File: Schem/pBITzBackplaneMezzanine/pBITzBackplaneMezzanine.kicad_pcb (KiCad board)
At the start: 4 copper layers, 139 x 130 mm, 52 parts, among them J1 USB3_A_Stacked, J2 Conn_01x04, J3 Conn_01x04, J4 10067847-001RLF, J5 FH69-60S-0.5SH, J6 pBITzBus, J7 FH69-60S-0.5SH, SW1 SW_Coded_SH-7030, SW2 SW_Coded_SH-7030, U1 FE1.1S-BSOP28BCN, U2 MAX3421EETJ_T, U3 CD74HC4050M96, U4 CD74HC4050M96, U5 74HC688, U6 74HC688, Y1 ABL-12.000MHZ-B2, Y2 ABL-12.000MHZ-B2

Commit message: synching
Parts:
- J2, J3: footprint Connector_PinSocket_2.54mm:PinSocket_1x04_P2.54mm_Vertical -> Connector_PinHeader_2.54mm:PinHeader_1x04_P2.54mm_Vertical

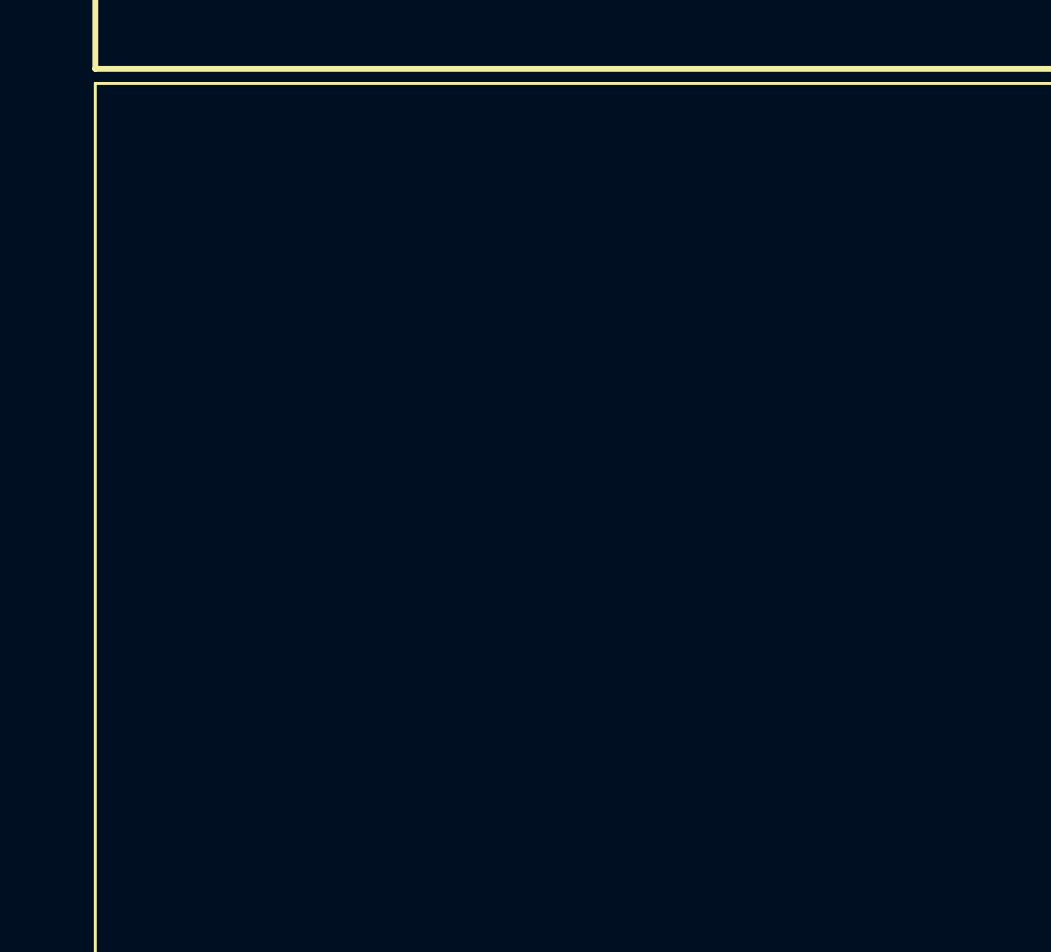
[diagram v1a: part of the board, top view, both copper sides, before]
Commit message: Added all the manufacturer part numbers to the KiCad schematics and PCB files. This will make it easier to order the parts for the project and ensure that the correct components are used. I also removed some of the old schematics that were no longer needed, such as the BaudClock, ConsolePort, DeviceSelectDecode, GPIOUserSerial, IO Controller, UserPorts, Video, and Z80HomeBrew schematics. These changes will help to streamline the design and make it easier to understand.
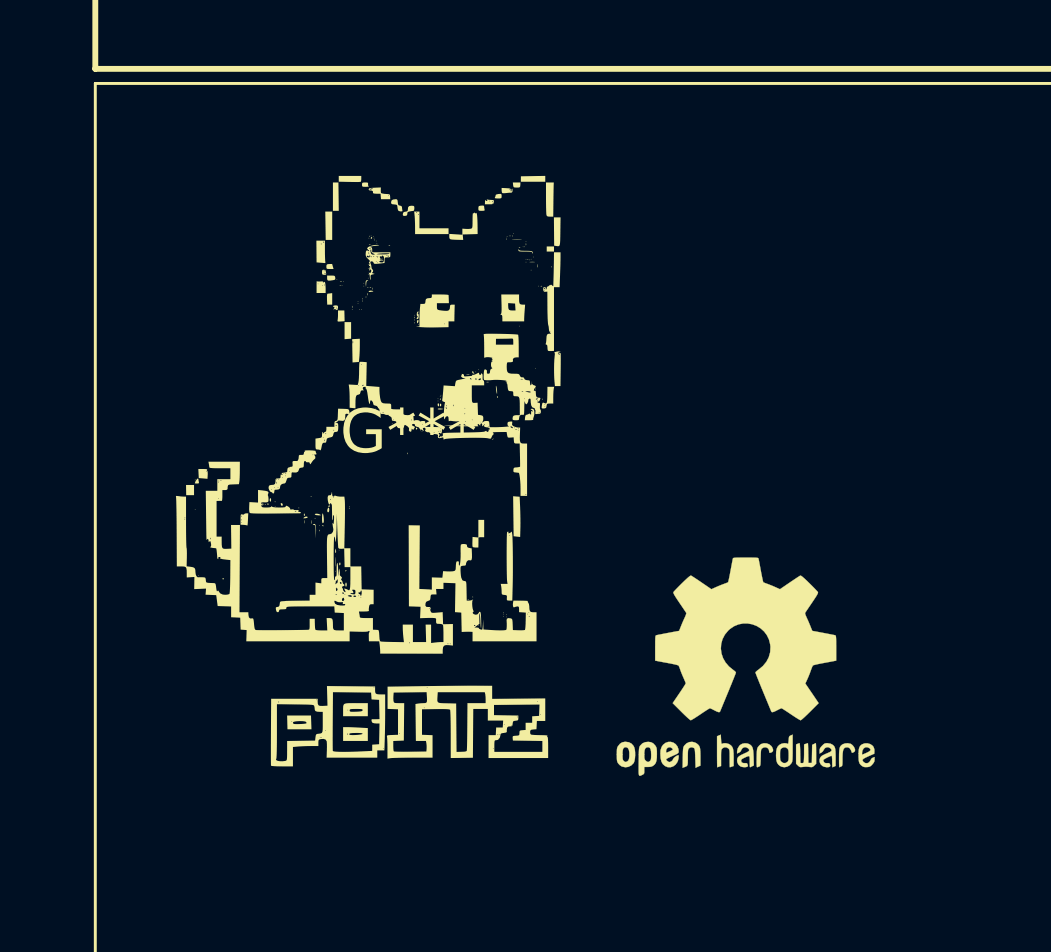
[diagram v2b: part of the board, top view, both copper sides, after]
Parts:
- added G***: LOGO, Footprints:pBITzlogo-Silk, F.Cu at (329.5, 232.5)
- added REF**: OSHW-Logo2_9.8x8mm_SilkScreen, Symbol:OSHW-Logo2_9.8x8mm_SilkScreen, F.Cu at (341.0, 240.5)

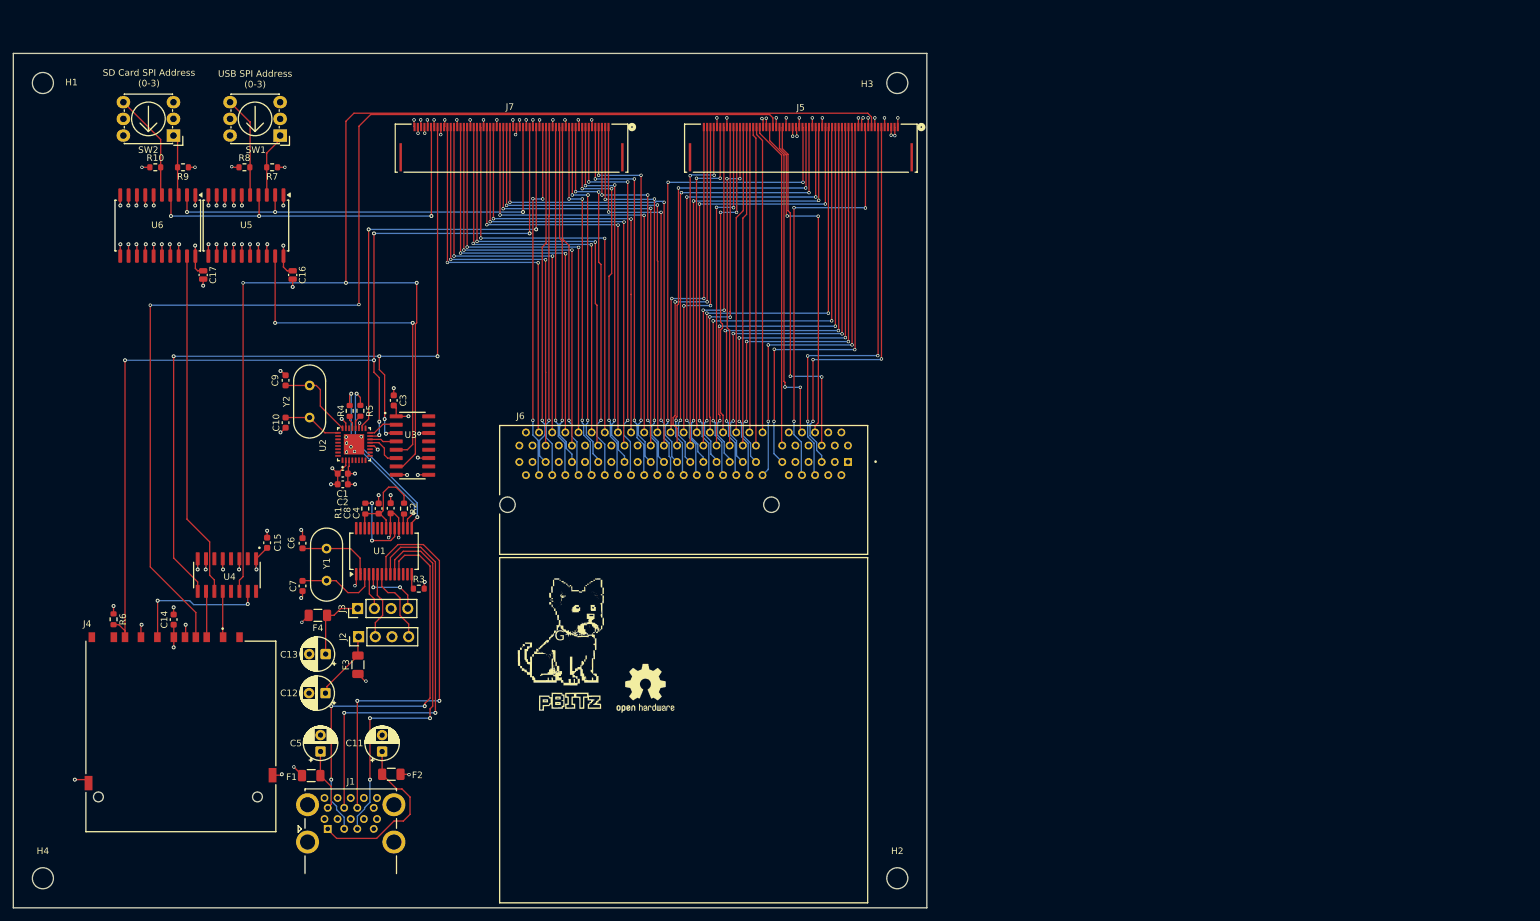
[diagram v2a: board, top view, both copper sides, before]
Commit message: * Corrected the reversal of the flat connector cable  * Added copper pours
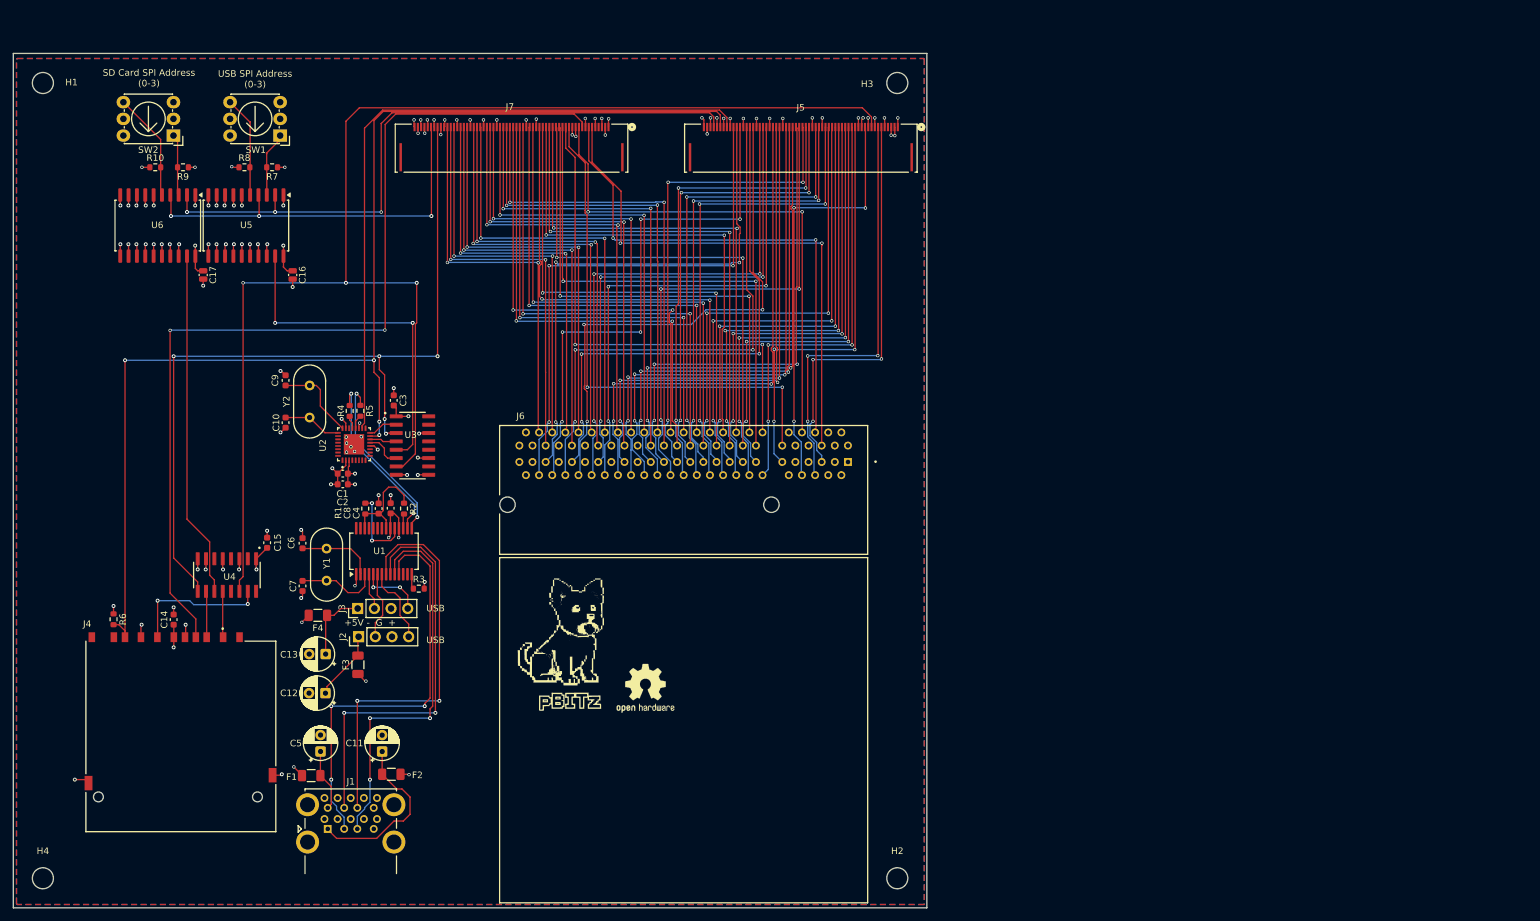
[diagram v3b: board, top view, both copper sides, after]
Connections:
- J5 pad 31: GND -> /MezzanineConnector/D11
- J5 pad 32: +5V -> /MezzanineConnector/D12
- J5 pad 33: +5V -> /MezzanineConnector/D13
- J5 pad 34: unconnected-(J5-Pad34) -> /MezzanineConnector/D14
- J5 pad 35: GND -> /MezzanineConnector/D15
- J5 pad 36: /MezzanineConnector/CLK0 -> GND
- J5 pad 37: /MezzanineConnector/CLK1 -> /MezzanineConnector/A12
- J5 pad 38: GND -> /MezzanineConnector/A13
- J5 pad 39: /MezzanineConnector/SPI_CD -> /MezzanineConnector/A14
- J5 pad 40: /MezzanineConnector/CART -> GND
- J5 pad 41: +3V3 -> /MezzanineConnector/A15
- J5 pad 42: +3V3 -> /MezzanineConnector/A16
- J5 pad 43: /MezzanineConnector/~{RESET} -> /MezzanineConnector/A17
- J5 pad 44: /MezzanineConnector/CTRL_1 -> GND
- J5 pad 45: /MezzanineConnector/CTRL_2 -> /MezzanineConnector/A18
- J5 pad 46: /MezzanineConnector/CTRL_3 -> /MezzanineConnector/A19
- J5 pad 47: /MezzanineConnector/CTRL_4 -> /MezzanineConnector/A20
- J5 pad 48: /MezzanineConnector/CTRL_5 -> GND
- J5 pad 49: /MezzanineConnector/CTRL_6 -> /MezzanineConnector/A21
- J5 pad 50: /MezzanineConnector/CTRL_7 -> /MezzanineConnector/A22
- J5 pad 51: /MezzanineConnector/CTRL_8 -> /MezzanineConnector/A23
- J5 pad 52: /MezzanineConnector/CTRL_9 -> GND
- J5 pad 53: GND -> /MezzanineConnector/~{SPI_INT}
- J5 pad 54: /MezzanineConnector/CS0 -> GND
- J5 pad 55: /MezzanineConnector/CS1 -> /MezzanineConnector/MISO
- J5 pad 57: /MezzanineConnector/D0 -> /MezzanineConnector/SPI_CS0
- J5 pad 58: /MezzanineConnector/D1 -> GND
- J5 pad 59: /MezzanineConnector/D2 -> GND
- J5 pad 60: /MezzanineConnector/D3 -> GND
- J7 pad 1: /MezzanineConnector/D11 -> GND
- J7 pad 10: GND -> /MezzanineConnector/CART
- J7 pad 11: /MezzanineConnector/A15 -> +3V3
- J7 pad 12: /MezzanineConnector/A16 -> +3V3
- J7 pad 13: /MezzanineConnector/A17 -> /MezzanineConnector/~{RESET}
- J7 pad 14: GND -> /MezzanineConnector/CTRL_1
- J7 pad 15: /MezzanineConnector/A18 -> /MezzanineConnector/CTRL_2
- J7 pad 16: /MezzanineConnector/A19 -> /MezzanineConnector/CTRL_3
- J7 pad 17: /MezzanineConnector/A20 -> /MezzanineConnector/CTRL_4
- J7 pad 18: GND -> /MezzanineConnector/CTRL_5
- J7 pad 19: /MezzanineConnector/A21 -> /MezzanineConnector/CTRL_6
- J7 pad 2: /MezzanineConnector/D12 -> +5V
- J7 pad 20: /MezzanineConnector/A22 -> /MezzanineConnector/CTRL_7
- J7 pad 21: /MezzanineConnector/A23 -> /MezzanineConnector/CTRL_8
- J7 pad 22: GND -> /MezzanineConnector/CTRL_9
- J7 pad 23: /MezzanineConnector/~{SPI_INT} -> GND
- J7 pad 24: GND -> /MezzanineConnector/CS0
- J7 pad 25: /MezzanineConnector/MISO -> /MezzanineConnector/CS1
- J7 pad 27: /MezzanineConnector/SPI_CS0 -> /MezzanineConnector/D0
- J7 pad 28: GND -> /MezzanineConnector/D1
- J7 pad 29: GND -> /MezzanineConnector/D2
- J7 pad 3: /MezzanineConnector/D13 -> +5V
- J7 pad 30: GND -> /MezzanineConnector/D3
- J7 pad 4: /MezzanineConnector/D14 -> unconnected-(J7-Pad4)
- J7 pad 5: /MezzanineConnector/D15 -> GND
- J7 pad 6: GND -> /MezzanineConnector/CLK0
- J7 pad 7: /MezzanineConnector/A12 -> /MezzanineConnector/CLK1
- J7 pad 8: /MezzanineConnector/A13 -> GND
- J7 pad 9: /MezzanineConnector/A14 -> /MezzanineConnector/SPI_CD
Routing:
- net /MezzanineConnector/SPI_CD: track 177.6 -> 144.2 mm
- net /MezzanineConnector/MISO: track 155.5 -> 188.1 mm, vias 6 -> 4
- net /MezzanineConnector/~{SPI_INT}: track 71.7 -> 104.0 mm, vias 2 -> 0
- net /MezzanineConnector/SPI_CS0: track 69.2 -> 101.3 mm
- net /MezzanineConnector/~{RESET}: track 49.9 -> 79.3 mm, vias 0 -> 2
- net /MezzanineConnector/CART: track 50.3 -> 79.6 mm
- net /MezzanineConnector/CTRL_2: track 48.6 -> 77.8 mm, vias 0 -> 2
- net /MezzanineConnector/CTRL_3: track 46.5 -> 75.3 mm, vias 0 -> 2
- net /MezzanineConnector/CTRL_1: track 46.8 -> 75.6 mm, vias 0 -> 2
- net /MezzanineConnector/A22: track 52.1 -> 80.3 mm, vias 1 -> 3
- net /MezzanineConnector/CTRL_4: track 48.7 -> 76.8 mm, vias 0 -> 2
- net /MezzanineConnector/CTRL_5: track 46.9 -> 74.4 mm, vias 0 -> 2
- net /MezzanineConnector/A20: track 53.6 -> 81.0 mm, vias 1 -> 3
- net /MezzanineConnector/A19: track 52.1 -> 79.4 mm, vias 1 -> 3
- net /MezzanineConnector/CLK0: track 53.7 -> 81.0 mm
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- added copper zone on B.Cu, net GND
- added copper zone on F.Cu, net GND
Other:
- board text added: "+5V - G +"
- board text added: "USB USB"

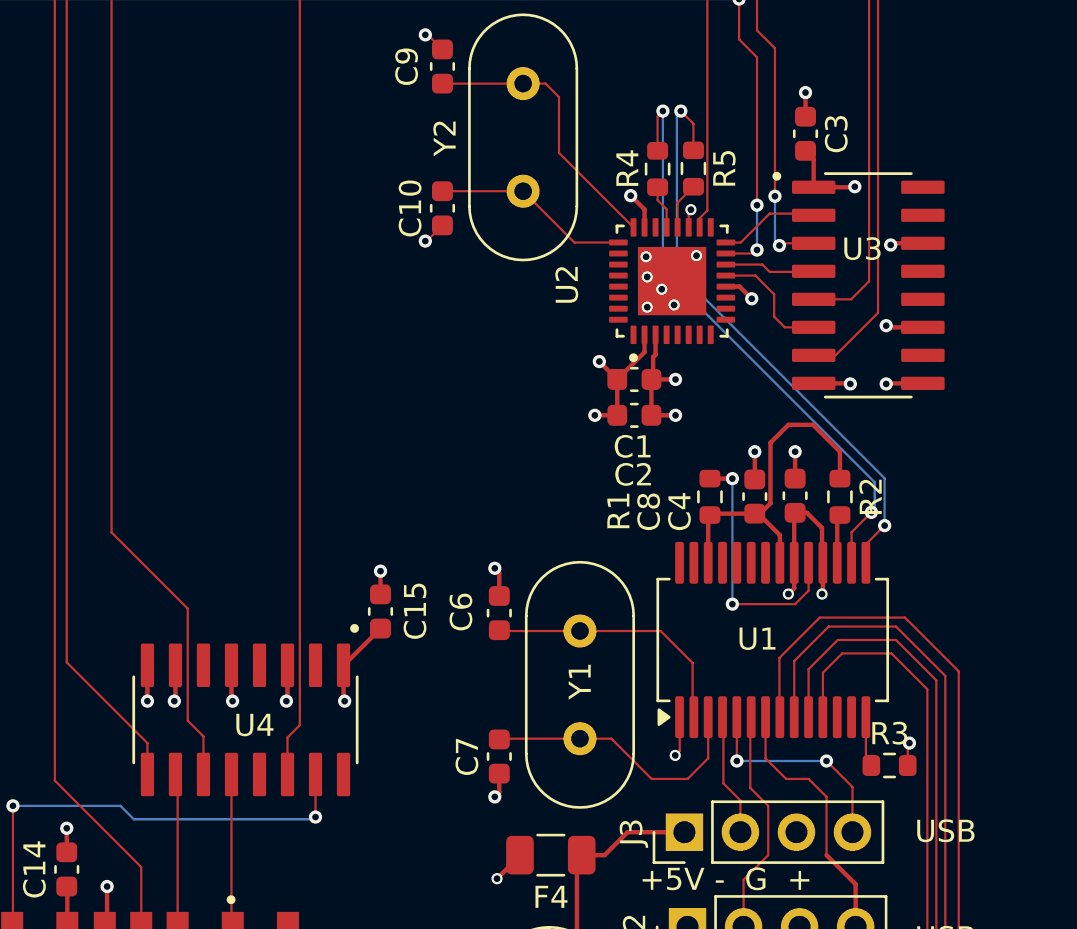
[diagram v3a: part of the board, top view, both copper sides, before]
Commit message: Updated the 3d images and exported the image
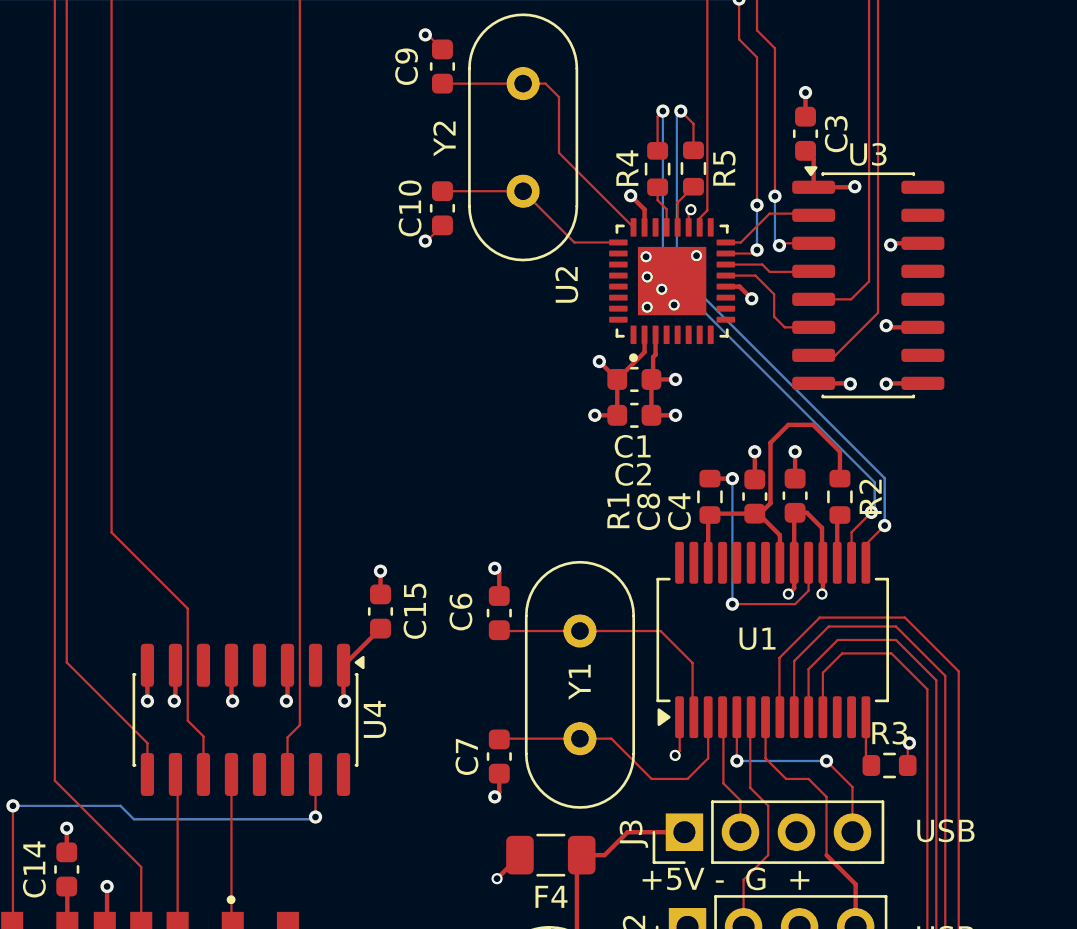
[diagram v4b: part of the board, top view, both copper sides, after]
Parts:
- U3, U4: footprint Footprints:SOIC127P600X175-16N -> Package_SO:SOIC-16_3.9x9.9mm_P1.27mm
